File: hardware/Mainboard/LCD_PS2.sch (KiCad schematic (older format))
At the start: 8 parts, among them T1 BC546, X4 KEYBOARD, X7 TIMER

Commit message: Misc: 	- Update README 	- Add 74HC138 datasheet 	- Update board image 	- Add layout for website tutorial
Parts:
- X2: renamed from X7; Mfr. Amphenol FCI -> TE Connectivity / AMP; Mfr. No. 68000-404HLF -> 826926-4; Mouser 649-68000-404HLF -> 571-826926-4
- renumbered R13 to R1, R10 to R2, R12 to R3, X4 to X3
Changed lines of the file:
@@
 AR Path="/5DAE0AEC" Ref="#PWR?"  Part="1"
 AR Path="/5EB09E21/5DAE0AEC" Ref="#PWR?"  Part="1"
-AR Path="/5DADBF97/5DAE0AEC" Ref="#PWR066"  Part="1"
-F 0 "#PWR066" H 5075 3375 50  0001 C CNN
+AR Path="/5DADBF97/5DAE0AEC" Ref="#PWR012"  Part="1"
+F 0 "#PWR012" H 5075 3375 50  0001 C CNN
 F 1 "GND" H 5080 3452 50  0000 C CNN
 F 2 "" H 5075 3625 50  0001 C CNN
@@
 AR Path="/5DE9A843" Ref="#PWR?"  Part="1"
 AR Path="/5EB09E21/5DE9A843" Ref="#PWR?"  Part="1"
-AR Path="/5DADBF97/5DE9A843" Ref="#PWR069"  Part="1"
-F 0 "#PWR069" H 6125 2150 50  0001 C CNN
+AR Path="/5DADBF97/5DE9A843" Ref="#PWR017"  Part="1"
+F 0 "#PWR017" H 6125 2150 50  0001 C CNN
 F 1 "GND" H 6130 2227 50  0000 C CNN
 F 2 "" H 6125 2400 50  0001 C CNN
@@
 AR Path="/5DE9C02E" Ref="#PWR?"  Part="1"
 AR Path="/5EB09E21/5DE9C02E" Ref="#PWR?"  Part="1"
-AR Path="/5DADBF97/5DE9C02E" Ref="#PWR068"  Part="1"
-F 0 "#PWR068" H 5625 2275 50  0001 C CNN
+AR Path="/5DADBF97/5DE9C02E" Ref="#PWR015"  Part="1"
+F 0 "#PWR015" H 5625 2275 50  0001 C CNN
 F 1 "+5V" H 5640 2598 50  0000 C CNN
 F 2 "" H 5625 2425 50  0001 C CNN
@@
 AR Path="/5DADFE9B" Ref="#PWR?"  Part="1"
 AR Path="/5EB09E21/5DADFE9B" Ref="#PWR?"  Part="1"
-AR Path="/5DADBF97/5DADFE9B" Ref="#PWR064"  Part="1"
-F 0 "#PWR064" H 5075 1725 50  0001 C CNN
+AR Path="/5DADBF97/5DADFE9B" Ref="#PWR011"  Part="1"
+F 0 "#PWR011" H 5075 1725 50  0001 C CNN
 F 1 "+5V" H 5090 2048 50  0000 C CNN
 F 2 "" H 5075 1875 50  0001 C CNN
@@
 LCD[0..11]
 $Comp
-L Connector_Custom:Mini-DIN-6 X4
+L Connector_Custom:Mini-DIN-6 X3
 U 1 1 5DD571A9
 P 5550 5550
-F 0 "X4" H 5550 5917 50  0000 C CNN
+F 0 "X3" H 5550 5917 50  0000 C CNN
 F 1 "KEYBOARD" H 5550 5826 50  0000 C CNN
 F 2 "Connector_Custom:Mini-DIN_TE_Female_6Pin_2rows" H 5550 5550 50  0001 C CNN
@@
 AR Path="/5DD5A54C" Ref="#PWR?"  Part="1"
 AR Path="/5EB09E21/5DD5A54C" Ref="#PWR?"  Part="1"
-AR Path="/5DADBF97/5DD5A54C" Ref="#PWR073"  Part="1"
-F 0 "#PWR073" H 5075 5300 50  0001 C CNN
+AR Path="/5DADBF97/5DD5A54C" Ref="#PWR013"  Part="1"
+F 0 "#PWR013" H 5075 5300 50  0001 C CNN
 F 1 "+5V" H 5090 5623 50  0000 C CNN
 F 2 "" H 5075 5450 50  0001 C CNN
@@
 	4600 6350 4700 6450
 Wire Bus Line
-	4600 6050 2500 6050
-Text HLabel 2500 6050 0    50   BiDi ~ 0
+	4600 6050 1975 6050
+Text HLabel 1975 6050 0    50   BiDi ~ 0
 PS2[0..1]
 Wire Wire Line
@@
 AR Path="/5DA8A71B" Ref="#PWR?"  Part="1"
 AR Path="/5EB09E21/5DA8A71B" Ref="#PWR?"  Part="1"
-AR Path="/5DADBF97/5DA8A71B" Ref="#PWR0102"  Part="1"
-F 0 "#PWR0102" H 5550 5650 50  0001 C CNN
+AR Path="/5DADBF97/5DA8A71B" Ref="#PWR014"  Part="1"
+F 0 "#PWR014" H 5550 5650 50  0001 C CNN
 F 1 "GND" H 5555 5727 50  0000 C CNN
 F 2 "" H 5550 5900 50  0001 C CNN
@@
 U 1 1 5DE99AEE
 P 6125 2175
-F 0 "RV1" H 6055 2129 50  0000 R CNN
-F 1 "10k" H 6055 2220 50  0000 R CNN
+F 0 "RV1" V 6125 2250 50  0000 R CNN
+F 1 "10k" V 6025 2250 50  0000 R CNN
 F 2 "Potentiometer:Bourns_3386P_Vertical" H 6125 2175 50  0001 C CNN
 F 3 "https://www.mouser.de/datasheet/2/54/3386-776606.pdf" H 6125 2175 50  0001 C CNN
@@
 AR Path="/5DDCDE4D" Ref="#PWR?"  Part="1"
 AR Path="/5EB09E21/5DDCDE4D" Ref="#PWR?"  Part="1"
-AR Path="/5DADBF97/5DDCDE4D" Ref="#PWR0103"  Part="1"
-F 0 "#PWR0103" H 6125 5650 50  0001 C CNN
+AR Path="/5DADBF97/5DDCDE4D" Ref="#PWR018"  Part="1"
+F 0 "#PWR018" H 6125 5650 50  0001 C CNN
 F 1 "GND" H 6130 5727 50  0000 C CNN
 F 2 "" H 6125 5900 50  0001 C CNN
@@
 AR Path="/5E36C0FD" Ref="R?"  Part="1"
 AR Path="/5EB09E21/5E36C0FD" Ref="R?"  Part="1"
-AR Path="/5DADBF97/5E36C0FD" Ref="R10"  Part="1"
-F 0 "R10" V 4975 6025 50  0000 L CNN
+AR Path="/5DADBF97/5E36C0FD" Ref="R2"  Part="1"
+F 0 "R2" V 4975 6050 50  0000 L CNN
 F 1 "10k" V 4875 6025 50  0000 L CNN
 F 2 "Resistor_THT:R_Axial_DIN0207_L6.3mm_D2.5mm_P7.62mm_Horizontal" V 4905 6100 50  0001 C CNN
@@
 AR Path="/5E36C658" Ref="R?"  Part="1"
 AR Path="/5EB09E21/5E36C658" Ref="R?"  Part="1"
-AR Path="/5DADBF97/5E36C658" Ref="R12"  Part="1"
-F 0 "R12" V 5075 6025 50  0000 L CNN
+AR Path="/5DADBF97/5E36C658" Ref="R3"  Part="1"
+F 0 "R3" V 5075 6050 50  0000 L CNN
 F 1 "10k" V 5175 6025 50  0000 L CNN
 F 2 "Resistor_THT:R_Axial_DIN0207_L6.3mm_D2.5mm_P7.62mm_Horizontal" V 5005 6100 50  0001 C CNN
@@
 AR Path="/5E36F16F" Ref="#PWR?"  Part="1"
 AR Path="/5EB09E21/5E36F16F" Ref="#PWR?"  Part="1"
-AR Path="/5DADBF97/5E36F16F" Ref="#PWR019"  Part="1"
-F 0 "#PWR019" H 5025 5700 50  0001 C CNN
+AR Path="/5DADBF97/5E36F16F" Ref="#PWR010"  Part="1"
+F 0 "#PWR010" H 5025 5700 50  0001 C CNN
 F 1 "+5V" H 5040 6023 50  0000 C CNN
 F 2 "" H 5025 5850 50  0001 C CNN
@@
 AR Path="/5E3B1822" Ref="#PWR?"  Part="1"
 AR Path="/5EB09E21/5E3B1822" Ref="#PWR?"  Part="1"
-AR Path="/5DADBF97/5E3B1822" Ref="#PWR065"  Part="1"
-F 0 "#PWR065" H 5625 4475 50  0001 C CNN
+AR Path="/5DADBF97/5E3B1822" Ref="#PWR016"  Part="1"
+F 0 "#PWR016" H 5625 4475 50  0001 C CNN
 F 1 "GND" H 5630 4552 50  0000 C CNN
 F 2 "" H 5625 4725 50  0001 C CNN
@@
 AR Path="/5E3B3B17" Ref="R?"  Part="1"
 AR Path="/5EB09E21/5E3B3B17" Ref="R?"  Part="1"
-AR Path="/5DADBF97/5E3B3B17" Ref="R13"  Part="1"
-F 0 "R13" V 4650 4150 50  0000 L CNN
-F 1 "4,7k" V 4550 4150 50  0000 L CNN
+AR Path="/5DADBF97/5E3B3B17" Ref="R1"  Part="1"
+F 0 "R1" V 4650 4175 50  0000 L CNN
+F 1 "4,7k" V 4750 4150 50  0000 L CNN
 F 2 "Resistor_THT:R_Axial_DIN0207_L6.3mm_D2.5mm_P7.62mm_Horizontal" V 4580 4225 50  0001 C CNN
 F 3 "https://www.mouser.de/datasheet/2/447/Yageo%20LR_MFP_2013-594635.pdf" H 4650 4225 50  0001 C CNN
@@
 AR Path="/5E3B5DDD" Ref="#PWR?"  Part="1"
 AR Path="/5EB09E21/5E3B5DDD" Ref="#PWR?"  Part="1"
-AR Path="/5DADBF97/5E3B5DDD" Ref="#PWR058"  Part="1"
-F 0 "#PWR058" H 4650 3850 50  0001 C CNN
+AR Path="/5DADBF97/5E3B5DDD" Ref="#PWR09"  Part="1"
+F 0 "#PWR09" H 4650 3850 50  0001 C CNN
 F 1 "+5V" H 4665 4173 50  0000 C CNN
 F 2 "" H 4650 4000 50  0001 C CNN
@@
 AR Path="/5E772A75" Ref="#PWR?"  Part="1"
 AR Path="/5EB09E21/5E772A75" Ref="#PWR?"  Part="1"
-AR Path="/5DADBF97/5E772A75" Ref="#PWR074"  Part="1"
-F 0 "#PWR074" H 2925 1225 50  0001 C CNN
+AR Path="/5DADBF97/5E772A75" Ref="#PWR08"  Part="1"
+F 0 "#PWR08" H 2925 1225 50  0001 C CNN
 F 1 "GND" H 2930 1302 50  0000 C CNN
 F 2 "" H 2925 1475 50  0001 C CNN
@@
 	1975 1175 2275 1175
 $Comp
-L Connector_Generic:Conn_01x04 X7
+L Connector_Generic:Conn_01x04 X2
 U 1 1 5E783A1F
 P 3200 1275
-F 0 "X7" H 3280 1267 50  0000 L CNN
+F 0 "X2" H 3280 1267 50  0000 L CNN
 F 1 "TIMER" H 3280 1176 50  0000 L CNN
 F 2 "Connector_PinHeader_2.54mm:PinHeader_1x04_P2.54mm_Vertical" H 3200 1275 50  0001 C CNN
-F 3 "https://www.mouser.de/datasheet/2/18/68000-1266375.pdf" H 3200 1275 50  0001 C CNN
-F 4 "Amphenol FCI" H 3200 1275 50  0001 C CNN "Mfr."
-F 5 "68000-404HLF" H 3200 1275 50  0001 C CNN "Mfr. No."
-F 6 "649-68000-404HLF" H 3200 1275 50  0001 C CNN "Mouser"
+F 3 "https://www.te.com/commerce/DocumentDelivery/DDEController?Action=srchrtrv&DocNm=826629&DocType=Customer+Drawing&DocLang=English&PartCntxt=826926-4&DocFormat=pdf" H 3200 1275 50  0001 C CNN
+F 4 "TE Connectivity / AMP" H 3200 1275 50  0001 C CNN "Mfr."
+F 5 "826926-4" H 3200 1275 50  0001 C CNN "Mfr. No."
+F 6 "571-826926-4" H 3200 1275 50  0001 C CNN "Mouser"
 	1    3200 1275
 	1    0    0    -1
@@
 AR Path="/5E78679F" Ref="#PWR?"  Part="1"
 AR Path="/5EB09E21/5E78679F" Ref="#PWR?"  Part="1"
-AR Path="/5DADBF97/5E78679F" Ref="#PWR076"  Part="1"
-F 0 "#PWR076" H 2925 925 50  0001 C CNN
+AR Path="/5DADBF97/5E78679F" Ref="#PWR07"  Part="1"
+F 0 "#PWR07" H 2925 925 50  0001 C CNN
 F 1 "GND" H 2930 1002 50  0000 C CNN
 F 2 "" H 2925 1175 50  0001 C CNN

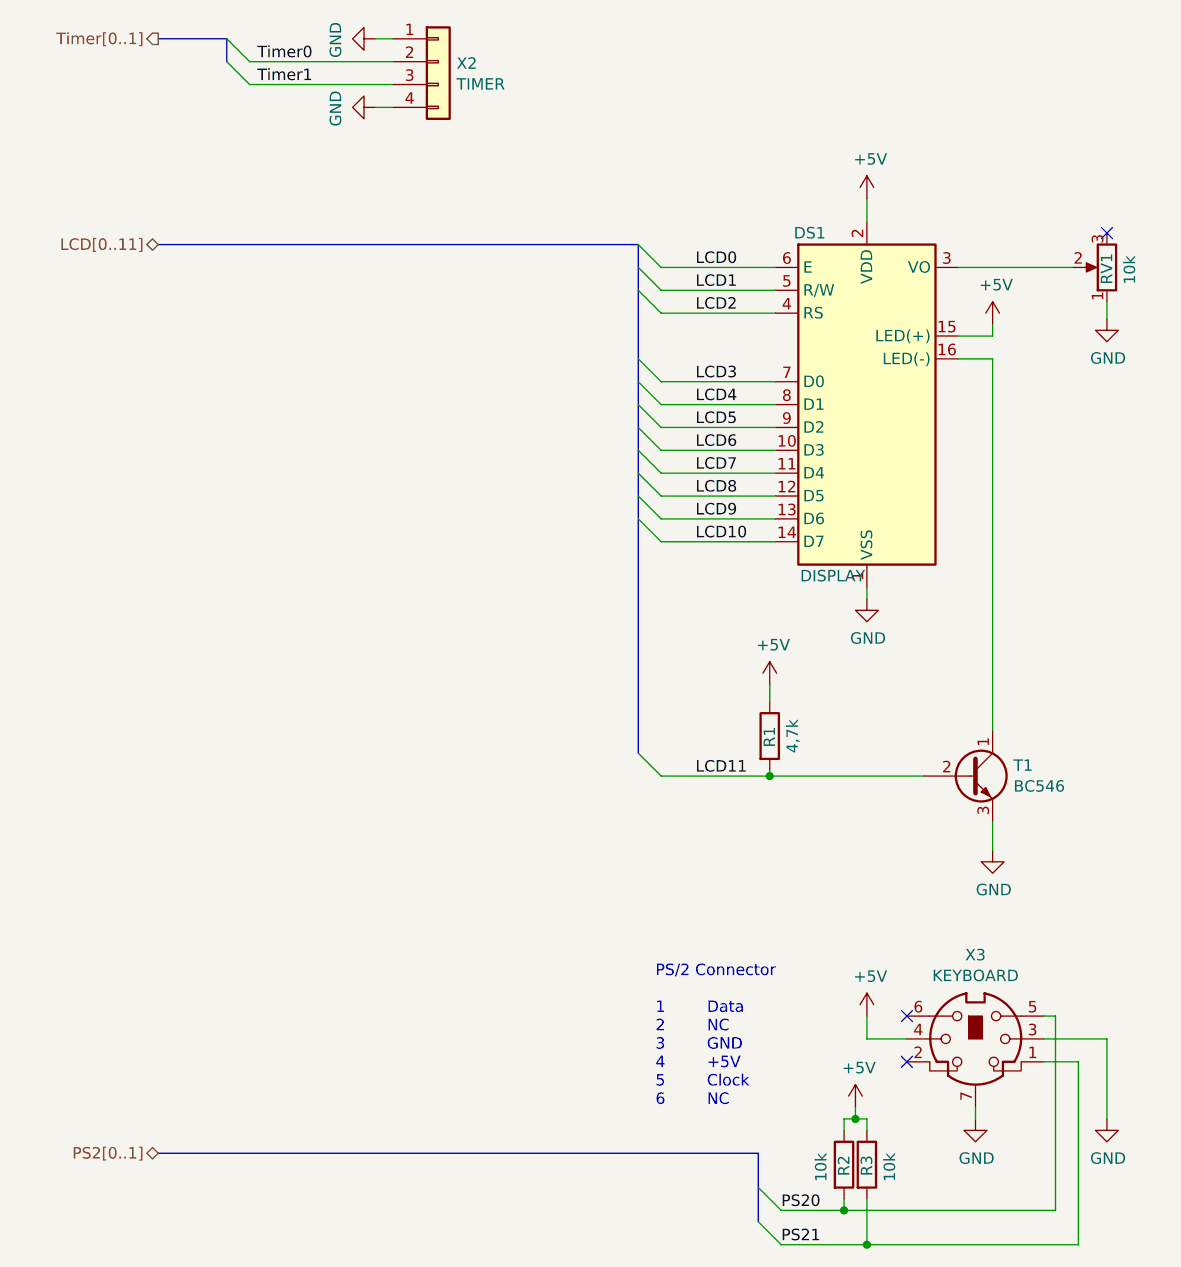
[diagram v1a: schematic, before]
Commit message: Hardware: 	- Add pull up resistor for PB
Documentation:
	- Add more datasheets
	- Update documentation

Misc:
	- Rename CHANGELOG
	- Remove old files

Signed-off-by: Daniel Kampert <DanielKampert@kampis-elektroecke.de>
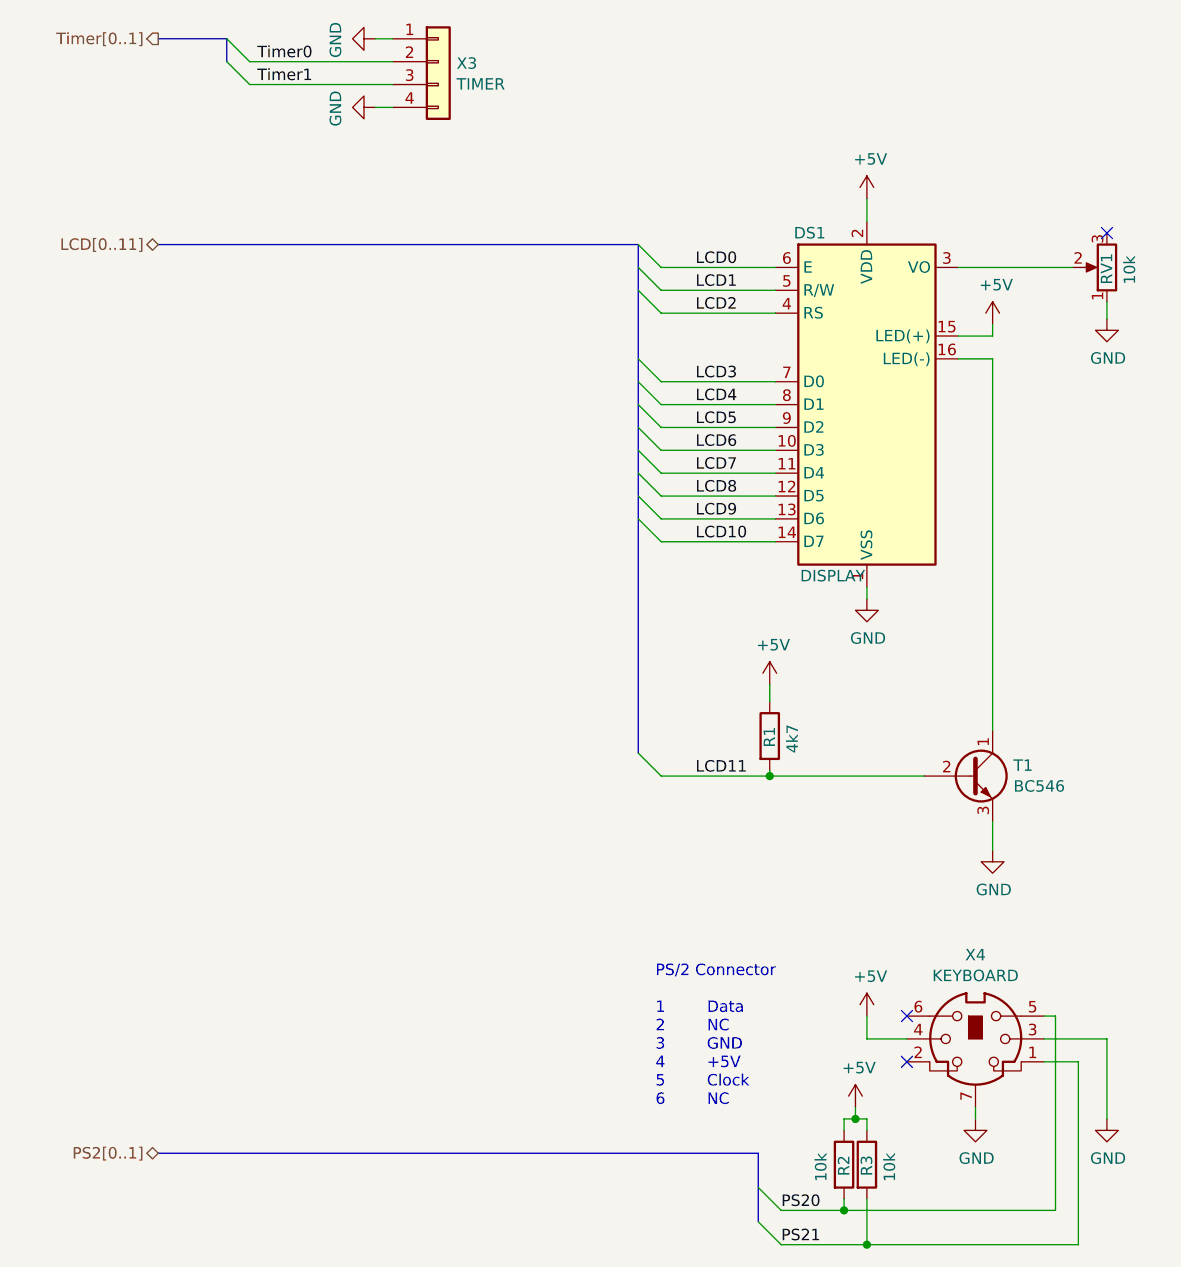
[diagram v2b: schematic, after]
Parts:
- DS1: Distributor (none) -> Mouser; Order Number (none) -> 763-0220GZ-FSW-GBW
- R1: value 4,7k -> 4k7; Distributor (none) -> Mouser; Order Number (none) -> 603-MFP-25BRD52-4K7
- R2, R3: Distributor (none) -> Mouser; Order Number (none) -> 603-MFP-25BRD52-10K
- RV1: Distributor (none) -> Mouser; Order Number (none) -> 652-3386Y-1-103LF
- T1: Distributor (none) -> Mouser; Order Number (none) -> 512-BC546CTA
- X3: renamed from X2; Distributor (none) -> Mouser; Order Number (none) -> 571-826926-4
- X4: renamed from X3; Distributor (none) -> Mouser; Order Number (none) -> 571-5749231-1
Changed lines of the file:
@@
 EESchema Schematic File Version 4
-LIBS:Mainboard-cache
 EELAYER 30 0
 EELAYER END
@@
 encoding utf-8
 Sheet 3 7
-Title "Mainboard"
-Date "2020-01-17"
+Title "LCD, P2/2 & Timer"
+Date "2020-10-11"
 Rev "1.0"
 Comp "https://www.kampis-elektroecke.de"
-Comment1 "Author: Daniel Kampert"
+Comment1 ""
 Comment2 ""
 Comment3 ""
-Comment4 "LCD, P2/2 & Timer"
+Comment4 "Author: Ing. Daniel Kampert"
 $EndDescr
 Wire Wire Line
@@
 AR Path="/5DAE0AEC" Ref="#PWR?"  Part="1"
 AR Path="/5EB09E21/5DAE0AEC" Ref="#PWR?"  Part="1"
-AR Path="/5DADBF97/5DAE0AEC" Ref="#PWR012"  Part="1"
-F 0 "#PWR012" H 5075 3375 50  0001 C CNN
+AR Path="/5DADBF97/5DAE0AEC" Ref="#PWR013"  Part="1"
+F 0 "#PWR013" H 5075 3375 50  0001 C CNN
 F 1 "GND" H 5080 3452 50  0000 C CNN
 F 2 "" H 5075 3625 50  0001 C CNN
@@
 AR Path="/5DE9A843" Ref="#PWR?"  Part="1"
 AR Path="/5EB09E21/5DE9A843" Ref="#PWR?"  Part="1"
-AR Path="/5DADBF97/5DE9A843" Ref="#PWR017"  Part="1"
-F 0 "#PWR017" H 6125 2150 50  0001 C CNN
+AR Path="/5DADBF97/5DE9A843" Ref="#PWR018"  Part="1"
+F 0 "#PWR018" H 6125 2150 50  0001 C CNN
 F 1 "GND" H 6130 2227 50  0000 C CNN
 F 2 "" H 6125 2400 50  0001 C CNN
@@
 AR Path="/5DE9C02E" Ref="#PWR?"  Part="1"
 AR Path="/5EB09E21/5DE9C02E" Ref="#PWR?"  Part="1"
-AR Path="/5DADBF97/5DE9C02E" Ref="#PWR015"  Part="1"
-F 0 "#PWR015" H 5625 2275 50  0001 C CNN
+AR Path="/5DADBF97/5DE9C02E" Ref="#PWR016"  Part="1"
+F 0 "#PWR016" H 5625 2275 50  0001 C CNN
 F 1 "+5V" H 5640 2598 50  0000 C CNN
 F 2 "" H 5625 2425 50  0001 C CNN
@@
 AR Path="/5DADFE9B" Ref="#PWR?"  Part="1"
 AR Path="/5EB09E21/5DADFE9B" Ref="#PWR?"  Part="1"
-AR Path="/5DADBF97/5DADFE9B" Ref="#PWR011"  Part="1"
-F 0 "#PWR011" H 5075 1725 50  0001 C CNN
+AR Path="/5DADBF97/5DADFE9B" Ref="#PWR012"  Part="1"
+F 0 "#PWR012" H 5075 1725 50  0001 C CNN
 F 1 "+5V" H 5090 2048 50  0000 C CNN
 F 2 "" H 5075 1875 50  0001 C CNN
@@
 LCD[0..11]
 $Comp
-L Connector_Custom:Mini-DIN-6 X3
+L Connector_Custom:Mini-DIN-6 X4
 U 1 1 5DD571A9
 P 5550 5550
-F 0 "X3" H 5550 5917 50  0000 C CNN
+F 0 "X4" H 5550 5917 50  0000 C CNN
 F 1 "KEYBOARD" H 5550 5826 50  0000 C CNN
 F 2 "Connector_Custom:Mini-DIN_TE_Female_6Pin_2rows" H 5550 5550 50  0001 C CNN
@@
 F 5 "5749231-1" H 5550 5550 50  0001 C CNN "Mfr. No."
 F 6 "571-5749231-1" H 5550 5550 50  0001 C CNN "Mouser"
+F 7 "Mouser" H 5550 5550 50  0001 C CNN "Distributor"
+F 8 "571-5749231-1" H 5550 5550 50  0001 C CNN "Order Number"
 	1    5550 5550
 	1    0    0    -1
@@
 AR Path="/5DD5A54C" Ref="#PWR?"  Part="1"
 AR Path="/5EB09E21/5DD5A54C" Ref="#PWR?"  Part="1"
-AR Path="/5DADBF97/5DD5A54C" Ref="#PWR013"  Part="1"
-F 0 "#PWR013" H 5075 5300 50  0001 C CNN
+AR Path="/5DADBF97/5DD5A54C" Ref="#PWR014"  Part="1"
+F 0 "#PWR014" H 5075 5300 50  0001 C CNN
 F 1 "+5V" H 5090 5623 50  0000 C CNN
 F 2 "" H 5075 5450 50  0001 C CNN
@@
 AR Path="/5DA8A71B" Ref="#PWR?"  Part="1"
 AR Path="/5EB09E21/5DA8A71B" Ref="#PWR?"  Part="1"
-AR Path="/5DADBF97/5DA8A71B" Ref="#PWR014"  Part="1"
-F 0 "#PWR014" H 5550 5650 50  0001 C CNN
+AR Path="/5DADBF97/5DA8A71B" Ref="#PWR015"  Part="1"
+F 0 "#PWR015" H 5550 5650 50  0001 C CNN
 F 1 "GND" H 5555 5727 50  0000 C CNN
 F 2 "" H 5550 5900 50  0001 C CNN
@@
 F 5 "3386Y-1-103LF" H 6125 2175 50  0001 C CNN "Mfr. No."
 F 6 "652-3386Y-1-103LF" H 6125 2175 50  0001 C CNN "Mouser"
+F 7 "Mouser" H 6125 2175 50  0001 C CNN "Distributor"
+F 8 "652-3386Y-1-103LF" H 6125 2175 50  0001 C CNN "Order Number"
 	1    6125 2175
 	-1   0    0    1
@@
 F 5 "NHD-0220GZ-FSW-GBW-L" H 5075 2775 50  0001 C CNN "Mfr. No."
 F 6 "763-0220GZ-FSW-GBW" H 5075 2775 50  0001 C CNN "Mouser"
+F 7 "Mouser" H 5075 2775 50  0001 C CNN "Distributor"
+F 8 "763-0220GZ-FSW-GBW" H 5075 2775 50  0001 C CNN "Order Number"
 	1    5075 2775
 	1    0    0    -1
@@
 AR Path="/5DDCDE4D" Ref="#PWR?"  Part="1"
 AR Path="/5EB09E21/5DDCDE4D" Ref="#PWR?"  Part="1"
-AR Path="/5DADBF97/5DDCDE4D" Ref="#PWR018"  Part="1"
-F 0 "#PWR018" H 6125 5650 50  0001 C CNN
+AR Path="/5DADBF97/5DDCDE4D" Ref="#PWR019"  Part="1"
+F 0 "#PWR019" H 6125 5650 50  0001 C CNN
 F 1 "GND" H 6130 5727 50  0000 C CNN
 F 2 "" H 6125 5900 50  0001 C CNN
@@
 F 5 "MFP-25BRD52-10K" H 4975 6100 50  0001 C CNN "Mfr. No."
 F 6 "603-MFP-25BRD52-10K" H 4975 6100 50  0001 C CNN "Mouser"
+F 7 "Mouser" H 4975 6100 50  0001 C CNN "Distributor"
+F 8 "603-MFP-25BRD52-10K" H 4975 6100 50  0001 C CNN "Order Number"
 	1    4975 6100
 	1    0    0    -1
@@
 F 5 "MFP-25BRD52-10K" H 5075 6100 50  0001 C CNN "Mfr. No."
 F 6 "603-MFP-25BRD52-10K" H 5075 6100 50  0001 C CNN "Mouser"
+F 7 "Mouser" H 5075 6100 50  0001 C CNN "Distributor"
+F 8 "603-MFP-25BRD52-10K" H 5075 6100 50  0001 C CNN "Order Number"
 	1    5075 6100
 	1    0    0    -1
@@
 AR Path="/5E36F16F" Ref="#PWR?"  Part="1"
 AR Path="/5EB09E21/5E36F16F" Ref="#PWR?"  Part="1"
-AR Path="/5DADBF97/5E36F16F" Ref="#PWR010"  Part="1"
-F 0 "#PWR010" H 5025 5700 50  0001 C CNN
+AR Path="/5DADBF97/5E36F16F" Ref="#PWR011"  Part="1"
+F 0 "#PWR011" H 5025 5700 50  0001 C CNN
 F 1 "+5V" H 5040 6023 50  0000 C CNN
 F 2 "" H 5025 5850 50  0001 C CNN
@@
 F 5 "BC546CTA" H 5525 4400 50  0001 C CNN "Mfr. No."
 F 6 "512-BC546CTA" H 5525 4400 50  0001 C CNN "Mouser"
+F 7 "Mouser" H 5525 4400 50  0001 C CNN "Distributor"
+F 8 "512-BC546CTA" H 5525 4400 50  0001 C CNN "Order Number"
 	1    5525 4400
 	1    0    0    -1
@@
 AR Path="/5E3B1822" Ref="#PWR?"  Part="1"
 AR Path="/5EB09E21/5E3B1822" Ref="#PWR?"  Part="1"
-AR Path="/5DADBF97/5E3B1822" Ref="#PWR016"  Part="1"
-F 0 "#PWR016" H 5625 4475 50  0001 C CNN
+AR Path="/5DADBF97/5E3B1822" Ref="#PWR017"  Part="1"
+F 0 "#PWR017" H 5625 4475 50  0001 C CNN
 F 1 "GND" H 5630 4552 50  0000 C CNN
 F 2 "" H 5625 4725 50  0001 C CNN
@@
 AR Path="/5DADBF97/5E3B3B17" Ref="R1"  Part="1"
 F 0 "R1" V 4650 4175 50  0000 L CNN
-F 1 "4,7k" V 4750 4150 50  0000 L CNN
+F 1 "4k7" V 4750 4150 50  0000 L CNN
 F 2 "Resistor_THT:R_Axial_DIN0207_L6.3mm_D2.5mm_P7.62mm_Horizontal" V 4580 4225 50  0001 C CNN
 F 3 "https://www.mouser.de/datasheet/2/447/Yageo%20LR_MFP_2013-594635.pdf" H 4650 4225 50  0001 C CNN
@@
 F 5 "MFP-25BRD52-4K7" H 4650 4225 50  0001 C CNN "Mfr. No."
 F 6 "603-MFP-25BRD52-4K7" H 4650 4225 50  0001 C CNN "Mouser"
+F 7 "Mouser" H 4650 4225 50  0001 C CNN "Distributor"
+F 8 "603-MFP-25BRD52-4K7" H 4650 4225 50  0001 C CNN "Order Number"
 	1    4650 4225
 	1    0    0    -1
@@
 AR Path="/5E3B5DDD" Ref="#PWR?"  Part="1"
 AR Path="/5EB09E21/5E3B5DDD" Ref="#PWR?"  Part="1"
-AR Path="/5DADBF97/5E3B5DDD" Ref="#PWR09"  Part="1"
-F 0 "#PWR09" H 4650 3850 50  0001 C CNN
+AR Path="/5DADBF97/5E3B5DDD" Ref="#PWR010"  Part="1"
+F 0 "#PWR010" H 4650 3850 50  0001 C CNN
 F 1 "+5V" H 4665 4173 50  0000 C CNN
 F 2 "" H 4650 4000 50  0001 C CNN
@@
 AR Path="/5E772A75" Ref="#PWR?"  Part="1"
 AR Path="/5EB09E21/5E772A75" Ref="#PWR?"  Part="1"
-AR Path="/5DADBF97/5E772A75" Ref="#PWR08"  Part="1"
-F 0 "#PWR08" H 2925 1225 50  0001 C CNN
+AR Path="/5DADBF97/5E772A75" Ref="#PWR09"  Part="1"
+F 0 "#PWR09" H 2925 1225 50  0001 C CNN
 F 1 "GND" H 2930 1302 50  0000 C CNN
 F 2 "" H 2925 1475 50  0001 C CNN
@@
 	1975 1175 2275 1175
 $Comp
-L Connector_Generic:Conn_01x04 X2
+L Connector_Generic:Conn_01x04 X3
 U 1 1 5E783A1F
 P 3200 1275
-F 0 "X2" H 3280 1267 50  0000 L CNN
+F 0 "X3" H 3280 1267 50  0000 L CNN
 F 1 "TIMER" H 3280 1176 50  0000 L CNN
 F 2 "Connector_PinHeader_2.54mm:PinHeader_1x04_P2.54mm_Vertical" H 3200 1275 50  0001 C CNN
@@
 F 5 "826926-4" H 3200 1275 50  0001 C CNN "Mfr. No."
 F 6 "571-826926-4" H 3200 1275 50  0001 C CNN "Mouser"
+F 7 "Mouser" H 3200 1275 50  0001 C CNN "Distributor"
+F 8 "571-826926-4" H 3200 1275 50  0001 C CNN "Order Number"
 	1    3200 1275
 	1    0    0    -1
@@
 AR Path="/5E78679F" Ref="#PWR?"  Part="1"
 AR Path="/5EB09E21/5E78679F" Ref="#PWR?"  Part="1"
-AR Path="/5DADBF97/5E78679F" Ref="#PWR07"  Part="1"
-F 0 "#PWR07" H 2925 925 50  0001 C CNN
+AR Path="/5DADBF97/5E78679F" Ref="#PWR08"  Part="1"
+F 0 "#PWR08" H 2925 925 50  0001 C CNN
 F 1 "GND" H 2930 1002 50  0000 C CNN
 F 2 "" H 2925 1175 50  0001 C CNN
